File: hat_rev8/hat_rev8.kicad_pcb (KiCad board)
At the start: 2 copper layers, 65 x 56 mm, 40 parts, among them J1 RPi 4, J6 DNP-Conn_01x05, J7 DNP-Conn_01x05, SW1 JOYSTICK, T1 BSS138, T2 BSS138, T3 BSS138, U1 SHT40, U2 TC1262-33

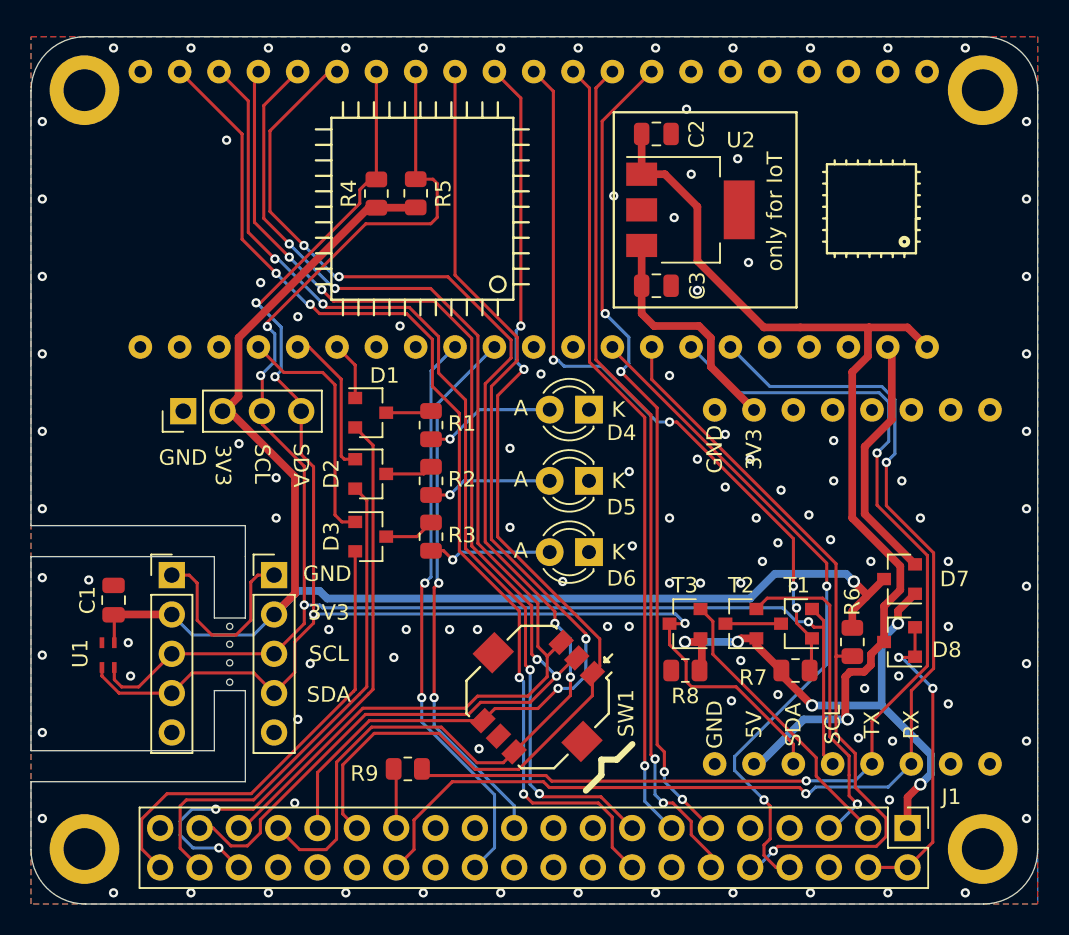
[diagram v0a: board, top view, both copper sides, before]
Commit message: remove old unneeded parts
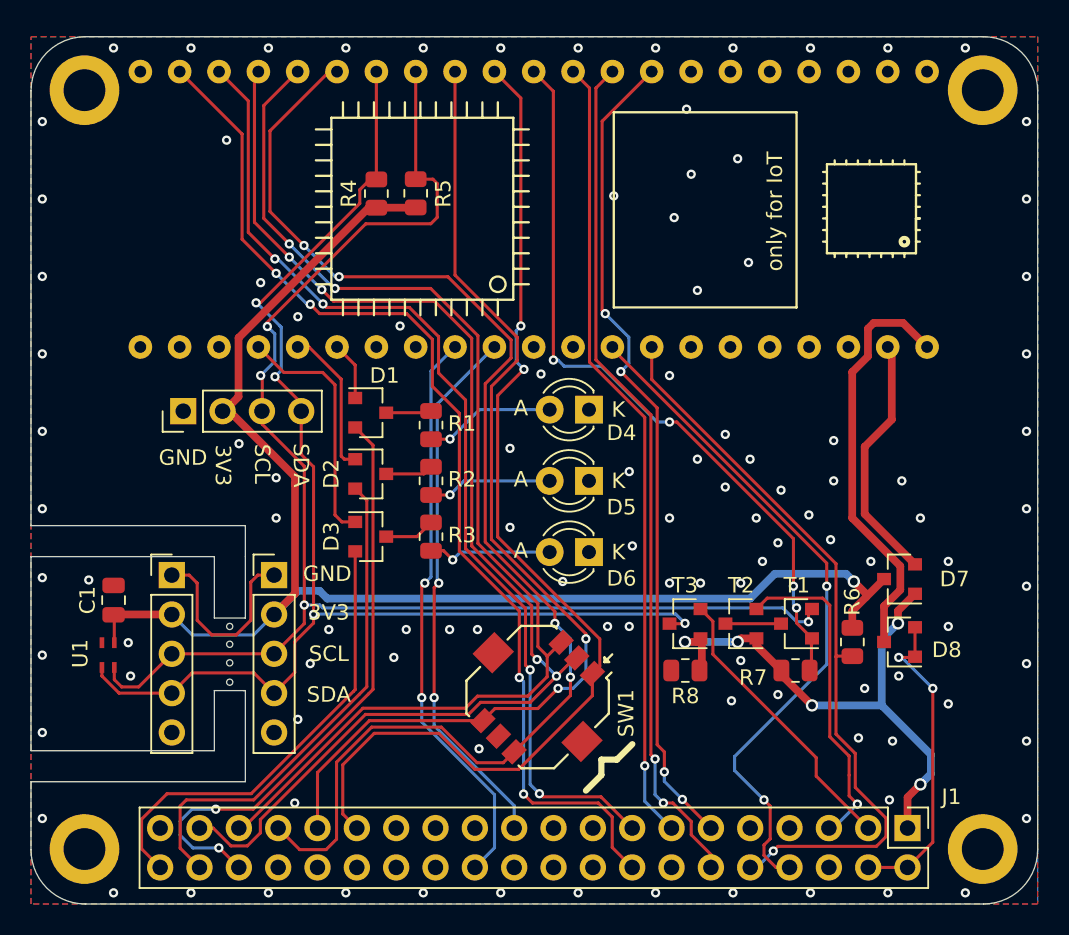
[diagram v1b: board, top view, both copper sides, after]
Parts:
- removed A3: mikroBUS, APROG_Footprints:mikroBUS
- removed C2, C3: 100nF, Capacitor_SMD:C_0805_2012Metric
- removed R9: 4k7, Resistor_SMD:R_0805_2012Metric
- removed U2: TC1262-33, Package_TO_SOT_SMD:SOT-223-3_TabPin2
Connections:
- A1 pad 1: Net-(A1-Pad1) -> unconnected-(A1-ADC1_DP0-Pad1)
- A1 pad 2: Net-(A1-Pad2) -> unconnected-(A1-ADCE_DM0-Pad2)
- A1 pad 23: Net-(A1-Pad23) -> unconnected-(A1-PTB19-Pad23)
- A1 pad 24: Net-(A1-Pad24) -> unconnected-(A1-PTC8-Pad24)
- A1 pad 28: Net-(A1-Pad28) -> unconnected-(A1-PTD0-Pad28)
- A1 pad 29: Net-(A1-Pad29) -> unconnected-(A1-PTD1-Pad29)
- A1 pad 3: Net-(A1-Pad3) -> unconnected-(A1-VREFH-Pad3)
- A1 pad 36: MB_TX -> Tiny_TX1
- A1 pad 37: MB_RX -> Tiny_RX1
- A1 pad 38: Net-(A1-Pad38) -> unconnected-(A1-ADC0_DP0-Pad38)
- A1 pad 39: Net-(A1-Pad39) -> unconnected-(A1-ADC0_DM0-Pad39)
- A1 pad 4: Net-(A1-Pad4) -> unconnected-(A1-VREFL/AGND-Pad4)
- A1 pad 5: Net-(A1-Pad5) -> unconnected-(A1-VREF_OUT-Pad5)
- A1 pad 6: Net-(A1-Pad6) -> unconnected-(A1-DAC-Pad6)
- A1 pad 7: Net-(A1-Pad7) -> unconnected-(A1-VBAT-Pad7)
- J1 pad 17: Net-(J1-Pad17) -> unconnected-(J1-Pin_17-Pad17)
- J1 pad 18: Net-(J1-Pad18) -> unconnected-(J1-Pin_18-Pad18)
- J1 pad 20: Net-(J1-Pad20) -> unconnected-(J1-Pin_20-Pad20)
- J1 pad 22: Net-(J1-Pad22) -> unconnected-(J1-Pin_22-Pad22)
- J1 pad 23: Net-(J1-Pad23) -> unconnected-(J1-Pin_23-Pad23)
- J1 pad 25: Net-(J1-Pad25) -> unconnected-(J1-Pin_25-Pad25)
- J1 pad 26: Net-(J1-Pad26) -> unconnected-(J1-Pin_26-Pad26)
- J1 pad 28: MB_RX -> RPI_RX_2
- J1 pad 32: Net-(J1-Pad32) -> unconnected-(J1-Pin_32-Pad32)
- J1 pad 7: Net-(J1-Pad7) -> unconnected-(J1-Pin_7-Pad7)
- J6 pad 5: Net-(J6-Pad5) -> unconnected-(J6-Pin_5-Pad5)
- J7 pad 5: Net-(J7-Pad5) -> unconnected-(J7-Pin_5-Pad5)
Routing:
- net MB_RX: track 75.4 -> 0.00 mm, vias 2 -> 0
- net MB_TX: track 70.6 -> 0.00 mm, vias 2 -> 0
- net +5V: track 64.4 -> 27.0 mm, vias 1 -> 0
- net +3V3_tiny: track 15.7 -> 0.00 mm
- net SDA: track 99.2 -> 85.2 mm
- net SCL: track 105.8 -> 95.0 mm
- net RPI_TX_2: track 3.89 -> 0.00 mm

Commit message: change PCB marking to V8
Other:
- board text added: "V8: 07/26"
- board text removed: "V7: JUL.2021"
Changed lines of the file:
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@@
 		)
 	)
-	(gr_text "V7: JUL.2021"
+	(gr_text "V8: 07/26"
 		(at 58.9 144.3 90)
 		(layer "F.Mask")

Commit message: add source file reference
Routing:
- net GND: vias 109 -> 103
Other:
- board text added: "Source Files:"
- board text removed: "only for IoT"
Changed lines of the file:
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@@
-	)
-	(gr_line
-		(start 92.8 124.8)
-		(end 92.8 137.4)
-		(stroke
-			(width 0.15)
-			(type solid)
-		)
-		(layer "F.SilkS")
-	)
-	(gr_line
-		(start 92.8 137.4)
-		(end 104.6 137.4)
-		(stroke
-			(width 0.15)
-			(type solid)
-		)
-		(layer "F.SilkS")
 	)
 	(gr_line
@@
 		(stroke
 			(width 0.4)
-			(type solid)
-		)
-		(layer "F.SilkS")
-	)
-	(gr_line
-		(start 104.6 124.8)
-		(end 92.8 124.8)
-		(stroke
-			(width 0.15)
-			(type solid)
-		)
-		(layer "F.SilkS")
-	)
-	(gr_line
-		(start 104.6 137.4)
-		(end 104.6 124.8)
-		(stroke
-			(width 0.15)
 			(type solid)
 		)
@@
 		)
 	)
-	(gr_text "only for IoT"
-		(at 103.2 131.2 90)
+	(gr_text "Source Files:"
+		(at 91.2 138.6 90)
 		(layer "F.SilkS")
 		(effects
 			(font
-				(size 1 1)
-				(thickness 0.15)
+				(size 1.5 1.5)
+				(thickness 0.3)
+				(bold yes)
 			)
+			(justify left bottom)
 		)
 	)
@@
 		)
 	)
+	(barcode
+		(at 99 131 0)
+		(layer "F.SilkS")
+		(size 13.6 13.6)
+		(text "https://hslu-aprog.github.io/aprog-hat/")
+		(text_height 1.5)
+		(type qr)
+		(ecc_level L)
+		(hide yes)
+		(knockout no)
+	)
 	(segment
 		(start 66.850001 158.550001)
@@
 	)
 	(via
-		(at 96.7 131.6)
-		(size 0.6)
-		(drill 0.3)
-		(layers "F.Cu" "B.Cu")
-		(capping no)
-		(covering
-			(front no)
-			(back no)
-		)
-		(plugging
-			(front no)
-			(back no)
-		)
-		(filling no)
-		(net "GND")
-	)
-	(via
 		(at 58.9 155)
 		(size 0.6)
@@
 	)
 	(via
-		(at 97.8 128.8)
-		(size 0.6)
-		(drill 0.3)
-		(layers "F.Cu" "B.Cu")
-		(capping no)
-		(covering
-			(front no)
-			(back no)
-		)
-		(plugging
-			(front no)
-			(back no)
-		)
-		(filling no)
-		(net "GND")
-	)
-	(via
 		(at 68.6 146.2)
 		(size 0.6)
@@
 	)
 	(via
-		(at 98.2 136.3)
-		(size 0.6)
-		(drill 0.3)
-		(layers "F.Cu" "B.Cu")
-		(capping no)
-		(covering
-			(front no)
-			(back no)
-		)
-		(plugging
-			(front no)
-			(back no)
-		)
-		(filling no)
-		(net "GND")
-	)
-	(via
 		(at 98.2 147.2)
 		(size 0.6)
@@
 	)
 	(via
-		(at 97.5 124.6)
-		(size 0.6)
-		(drill 0.3)
-		(layers "F.Cu" "B.Cu")
-		(capping no)
-		(covering
-			(front no)
-			(back no)
-		)
-		(plugging
-			(front no)
-			(back no)
-		)
-		(filling no)
-		(net "GND")
-	)
-	(via
 		(at 110.6 169.2)
 		(size 0.6)
@@
 	)
 	(via
-		(at 101.5 134.5)
-		(size 0.6)
-		(drill 0.3)
-		(layers "F.Cu" "B.Cu")
-		(capping no)
-		(covering
-			(front no)
-			(back no)
-		)
-		(plugging
-			(front no)
-			(back no)
-		)
-		(filling no)
-		(net "GND")
-	)
-	(via
 		(at 89.5 155.1)
 		(size 0.6)
@@
 		(size 0.6)
 		(drill 0.3)
-		(layers "F.Cu" "B.Cu")
-		(capping no)
-		(covering
-			(front no)
-			(back no)
-		)
-		(plugging
-			(front no)
-			(back no)
-		)
-		(filling no)
-		(net "GND")
-	)
-	(via
-		(at 100.8 127.8)
-		(size 0.6)
-		(drill 0.3)

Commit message: Finish v8
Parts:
- moved A2 37.8 mm to (102.8, 143.4)
- moved SW1 4.29 mm to (83.6, 162.8)
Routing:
- net SDA: track 85.2 -> 114.9 mm, vias 4 -> 6
- net SCL: track 95.0 -> 123.8 mm, vias 4 -> 7
- net JOYSTICK_RIGHT: track 69.3 -> 58.8 mm
- net +3V3: track 94.0 -> 104.1 mm, vias 1 -> 2
- net JOYSTICK_DOWN: track 84.4 -> 76.1 mm
- net JOYSTICK_LEFT: track 67.4 -> 59.5 mm
- net JOYSTICK_UP: track 76.4 -> 69.2 mm
- net Net-(D4-A): track 8.45 -> 14.2 mm, vias 1 -> 2
- net Net-(D6-A): track 8.11 -> 13.5 mm, vias 1 -> 2
- net JOYSTICK_PUSH: track 81.5 -> 76.7 mm, vias 4 -> 2
- net GP_3: track 65.4 -> 70.2 mm
- net GP_4: track 69.4 -> 73.9 mm
- net SDA_Raspi: track 18.6 -> 21.4 mm
- net RPI_RX_4: track 34.9 -> 37.4 mm
- net RPI_TX_4: track 37.0 -> 39.1 mm
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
